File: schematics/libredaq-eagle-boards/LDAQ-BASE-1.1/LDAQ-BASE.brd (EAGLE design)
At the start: 130 x 101 mm, 111 parts, among them Q1 FDV301N, Q2 FDV301N, Q3 FDV301N, Q4 FDV301N, Q5 FDV301N, Q6 FDV301N, Q7 FDV301N, T1 FDN340P, U1 ATSAM3U1CB, U2 LM3671MF-3.3, U4 ISL3175, U6 MCP16322, U8 LMV321, X1 PJ-102A, Y1 12M

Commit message: update from local copy
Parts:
- removed D1: D1, diode:SMB
- removed U6: MCP16322, libredaq-comps:QFN16-3X3MM
- removed X1: PJ-102A, SmartPrj:POWERSUPPLY_DC-21MM
- added D2: FM4004W-W, FM4004W-W:DIOM5025X231N
- added J1: PJ-102A, PJ-102A:PJ-102AH
- added U3: TS30012-M050QFNR, TS30012-M050QFNR:QFN50P300X300X100-17N
- JP6: value SCREWTERMINAL-3.5MM-3 -> 691214110003; device libredaq-comps:SCREWTERMINAL-3.5MM-3 -> 691214110003:691214110003
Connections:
- removed net N$16: C10.2, L5.1, U6.1, U6.12, U6.13, U6.16
- new net FB_PWR5: C10.2, L5.1, U3.1, U3.12, U3.13, U3.16
- net +5V: now also U3.5; no longer U6.5
- net GND: now also J1.2, J1.3, U3.14, U3.15, U3.17; no longer U6.14, U6.15, U6.4, U6.EXT, X1.1, X1.3
- net N$17: now also U3.10; no longer U6.10
- net PWRIN: now also D2.2, J1.1; no longer D1.A, X1.2
- net VIN: now also D2.1, U3.11, U3.2, U3.3; no longer D1.C, U6.11, U6.2, U6.3
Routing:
- net N$16: track 29.1 -> 0.00 mm
- net FB_PWR5: track 0.00 -> 22.3 mm
- net GND: track 899.0 -> 885.3 mm

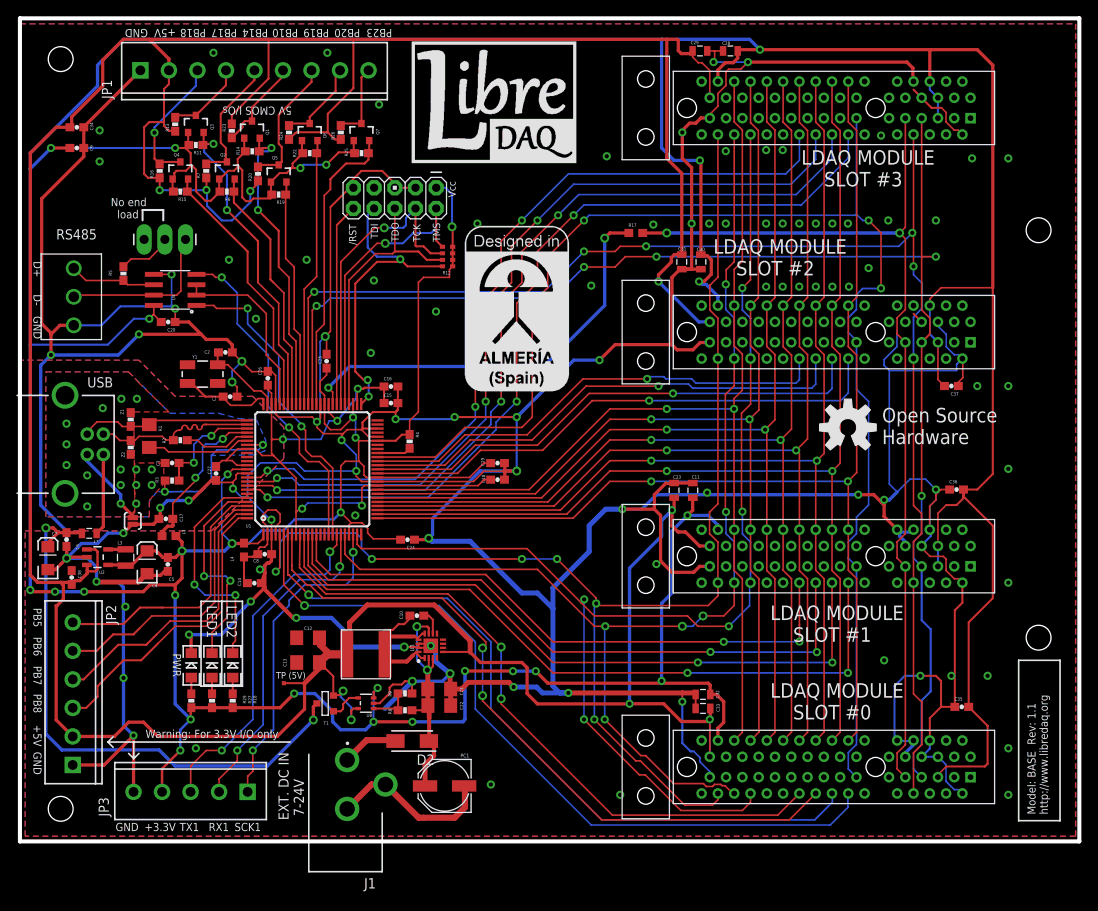
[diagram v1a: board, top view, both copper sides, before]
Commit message: base board: use bidirectional 3.3-5V driver
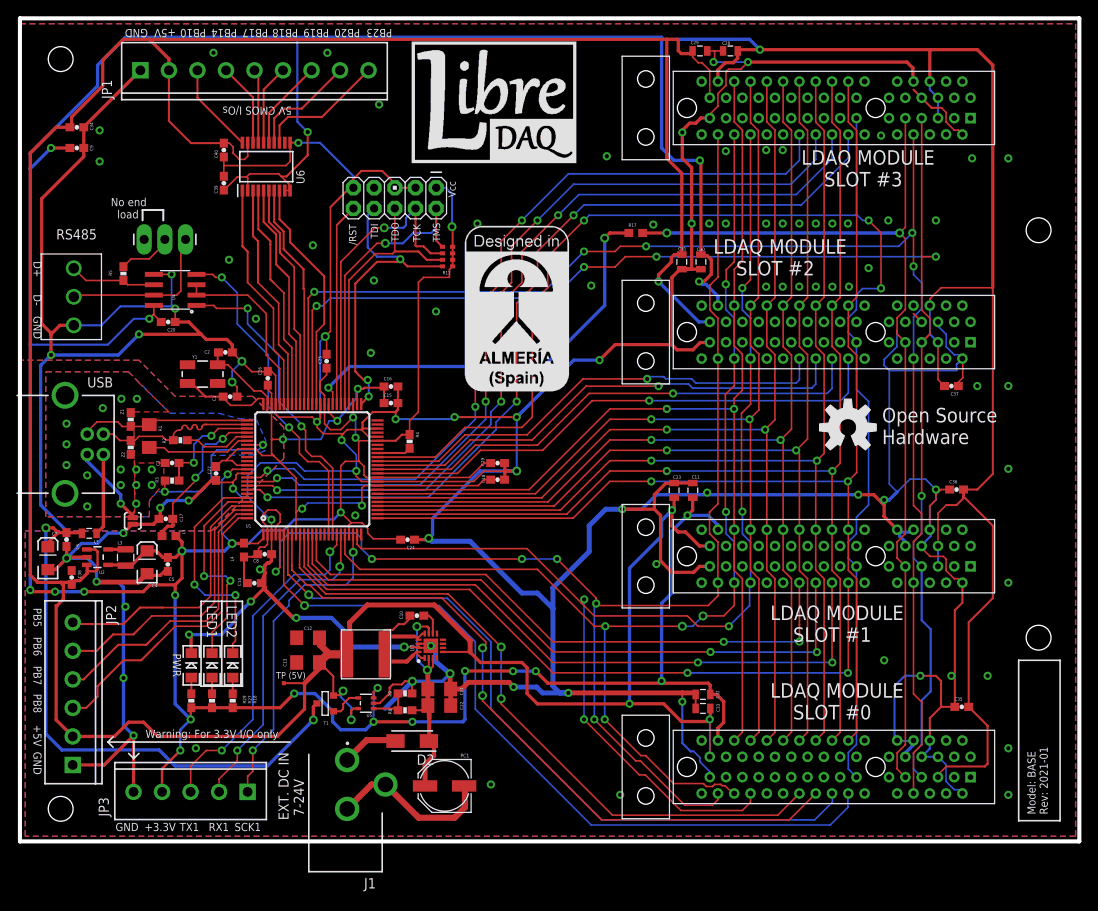
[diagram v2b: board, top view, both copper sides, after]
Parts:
- removed Q1, Q2, Q3, Q4, Q5, Q6, Q7: FDV301N, SparkFun:SOT23-3
- removed R11, R13, R14, R15, R16, R19, R20, R22, R23, R24, R25, R26, R6, R7: 10K, SparkFun:0603-RES
- added C39, C40: 0.1uF, SparkFun-Capacitors:0603-CAP
- added U6: TXB0108PWR, TXB0108PWR:SOP65P640X120-20N
- renumbered U8 to U5
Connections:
- net +5V: now also C40.1, U6.19; no longer R13.1, R16.1, R20.1, R23.1, R24.1, R26.1, R7.1
- net 3.3V: now also C39.1, U6.10, U6.2, U6.9; no longer Q1.1, Q2.1, Q3.1, Q4.1, Q5.1, Q6.1, Q7.1, R11.1, R14.1, R15.1, R19.1, R22.1, R25.1, R6.1
- net GND: now also C39.2, C40.2, U6.11
- net PB10_3.3: now also U6.1; no longer Q4.2, R15.2
- net PB10_5.0: now also JP1.3, U6.20; no longer JP1.6, Q1.3, R23.2
- net PB14_3.3: now also U6.3; no longer Q3.2, R11.2
- net PB14_5.0: now also JP1.4, U6.18; no longer JP1.5, Q2.3, R7.2
- net PB17_3.3: now also U6.4; no longer Q2.2, R6.2
- net PB17_5.0: now also JP1.5, U6.17; no longer JP1.4, Q3.3, R13.2
- net PB18_3.3: now also U6.5; no longer Q1.2, R14.2
- net PB18_5.0: now also JP1.6, U6.16; no longer JP1.3, Q4.3, R16.2
- net PB19_3.3: now also U6.6; no longer Q5.2, R19.2
- net PB19_5.0: now also U6.15; no longer Q5.3, R20.2
- net PB20_3.3: now also U6.7; no longer Q6.2, R22.2
- net PB20_5.0: now also U6.14; no longer Q6.3, R24.2
- net PB23_3.3: now also U6.8; no longer Q7.2, R25.2
- net PB23_5.0: now also U6.13; no longer Q7.3, R26.2
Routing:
- net +5V: track 467.6 -> 416.1 mm, vias 9 -> 6
- net 3.3V: track 779.4 -> 743.0 mm, vias 30 -> 28
- net GND: track 885.3 -> 909.2 mm, vias 99 -> 100
- net PB14_3.3: track 40.1 -> 28.0 mm, vias 2 -> 0
- net PB18_3.3: track 38.0 -> 27.9 mm, vias 2 -> 0
- net PB23_3.3: track 36.4 -> 28.9 mm
- net PB18_5.0: track 16.6 -> 9.86 mm, vias 1 -> 0
- net PB23_5.0: track 9.53 -> 15.8 mm
- net PB14_5.0: track 15.9 -> 10.3 mm
- net PB20_3.3: track 33.0 -> 27.7 mm
- net PB19_5.0: track 16.2 -> 11.0 mm
- net PB10_3.3: track 32.6 -> 28.3 mm
- net PB20_5.0: track 10.7 -> 14.3 mm
- net PB17_3.3: track 30.6 -> 27.9 mm
- net PB17_5.0: track 9.70 -> 9.07 mm
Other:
- board text added: "Model: BASE Rev: 2021-01"
- board text removed: "Model: BASE Rev: 1.1 http://www.libredaq.org"

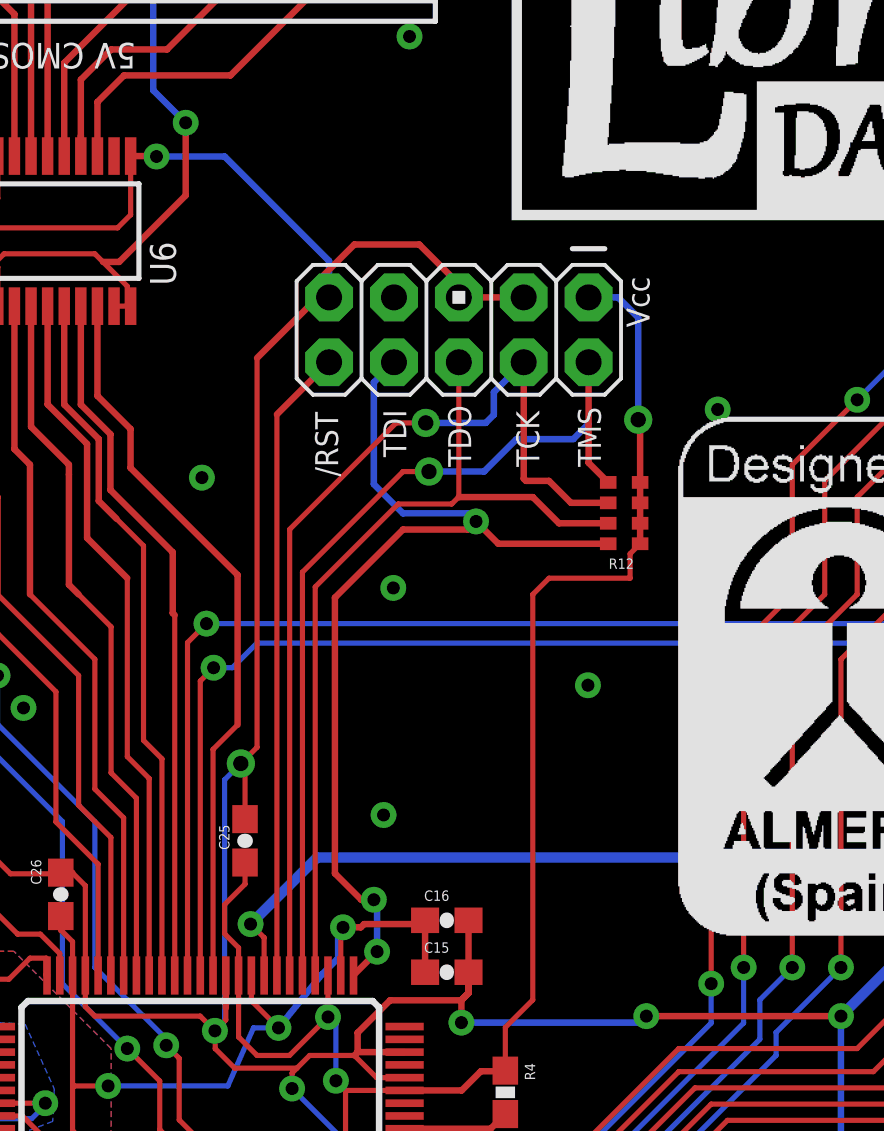
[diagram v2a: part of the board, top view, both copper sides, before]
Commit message: Base: Use JTAG 50mils connector
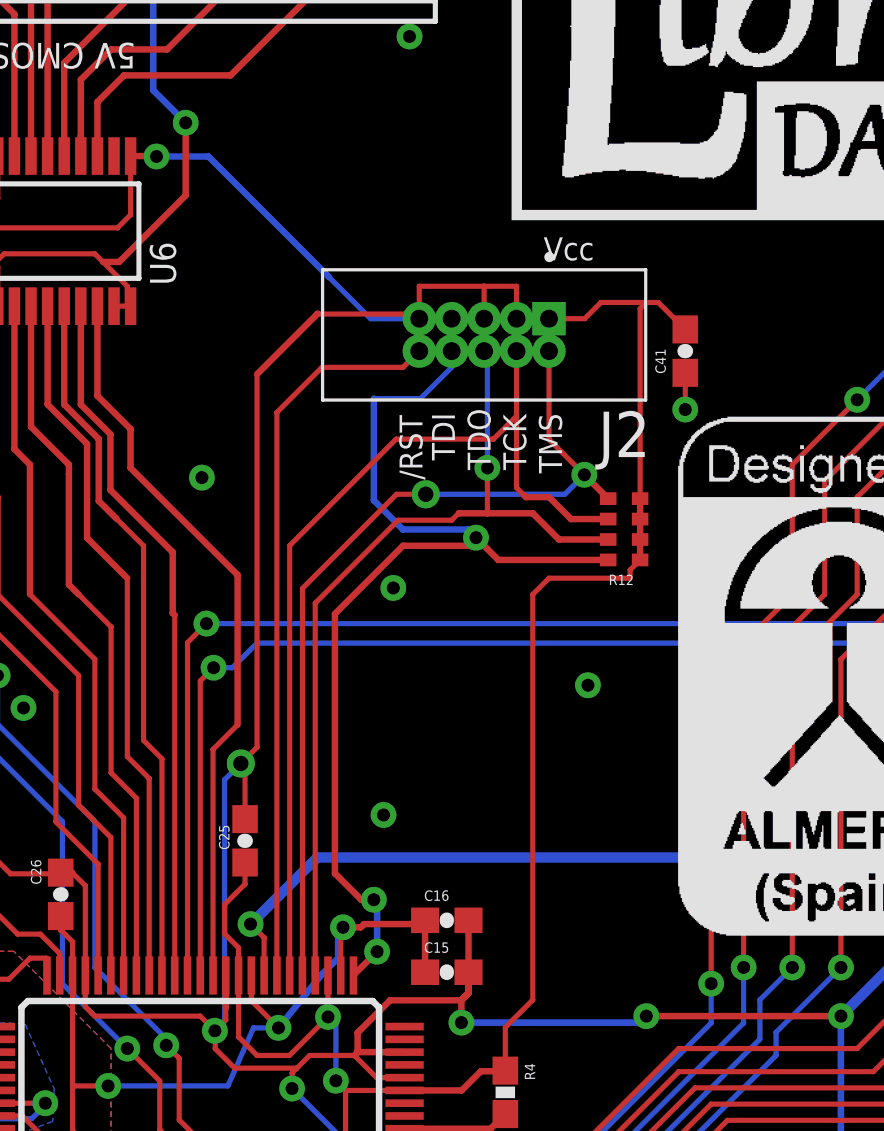
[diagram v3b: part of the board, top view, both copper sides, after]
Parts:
- removed JP4: SAM JTAG, SparkFun-Connectors:AVR_ICSP
- added C41: 0.1uF, SparkFun-Capacitors:0603-CAP
- added J2: 3221-10-0100-00, 3221-10-0100-00:CNC_3221-10-0100-00
- moved R12 0.64 mm to (52.5, 71.1)
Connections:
- net !JTAG_RESET: now also J2.10; no longer JP4.10
- net 3.3V: now also C41.2, J2.1; no longer JP4.1
- net GND: now also C41.1, J2.3, J2.5, J2.9; no longer JP4.3, JP4.5, JP4.9
- net JTAG_TCK: now also J2.4; no longer JP4.4
- net JTAG_TDI: now also J2.8; no longer JP4.8
- net JTAG_TDO: now also J2.6; no longer JP4.6
- net JTAG_TMS: now also J2.2; no longer JP4.2
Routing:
- net GND: track 909.2 -> 913.8 mm
- net 3.3V: track 743.0 -> 747.4 mm, vias 28 -> 27
- net !JTAG_RESET: track 24.9 -> 28.6 mm
- net JTAG_TMS: track 36.8 -> 34.8 mm, vias 1 -> 2
- net JTAG_TDI: track 38.5 -> 40.6 mm
- net JTAG_TCK: track 38.1 -> 37.3 mm, vias 1 -> 0
- net JTAG_TDO: track 33.8 -> 34.3 mm, vias 0 -> 1

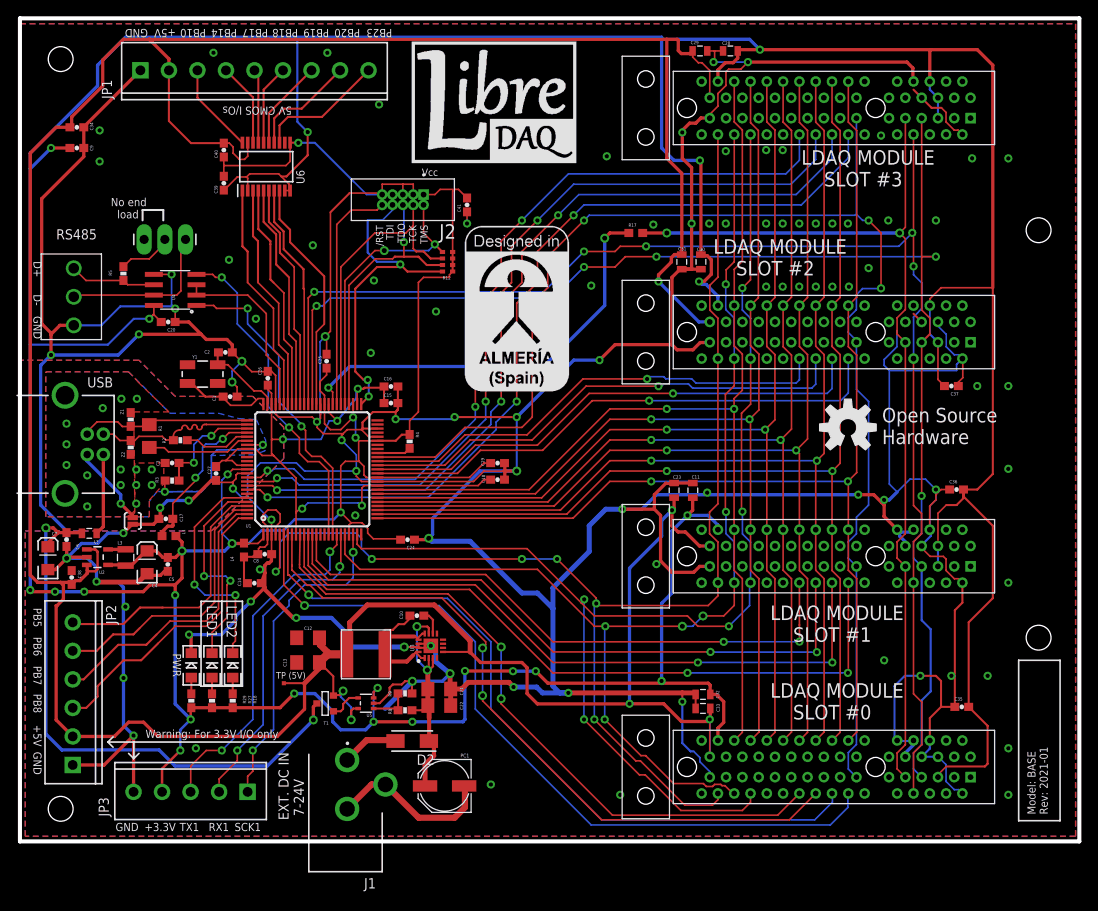
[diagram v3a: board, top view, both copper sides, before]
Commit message: Update connectors in BASE
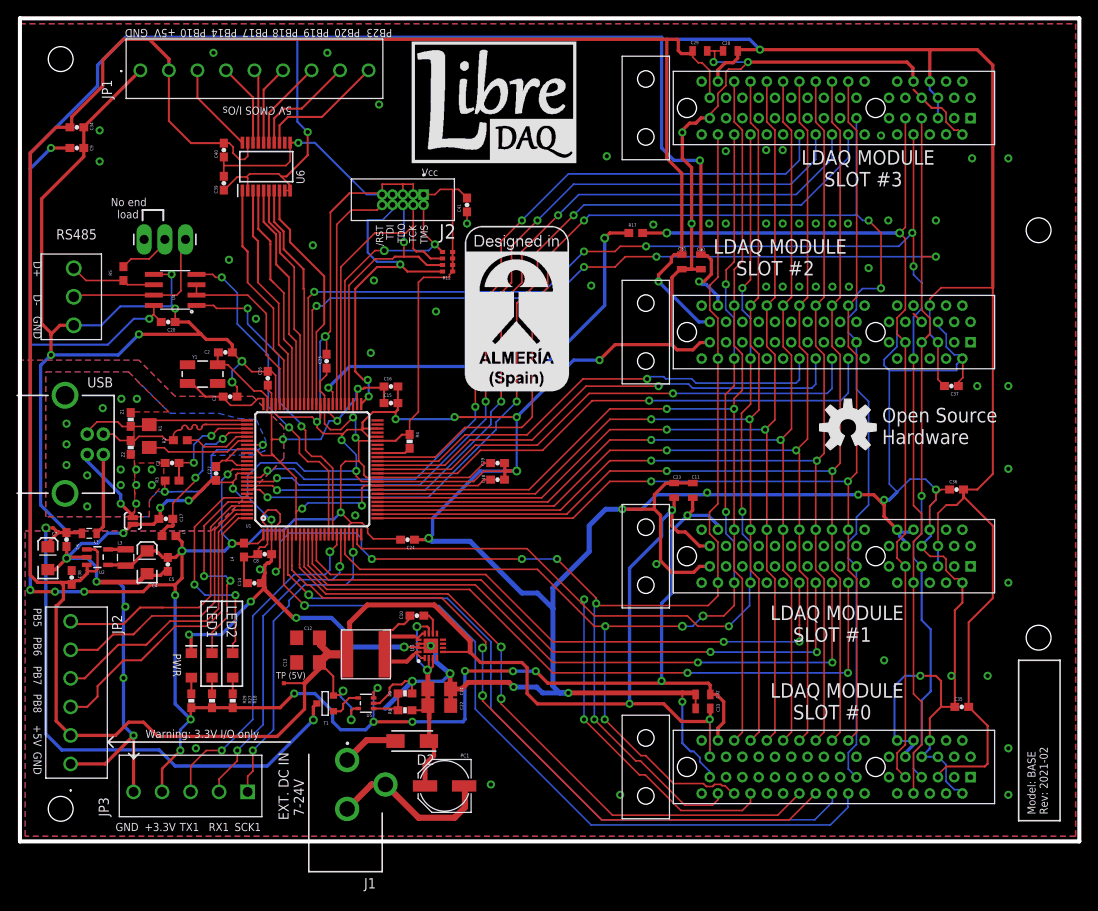
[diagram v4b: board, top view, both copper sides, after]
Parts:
- JP1: value SCREWTERMINAL-3.5MM-9 -> 39357-0009; device libredaq-comps:SCREWTERMINAL-3.5MM-9 -> SamacSys_Parts:393570009
- JP2: value SCREWTERMINAL-3.5MM-6 -> 1984659; device libredaq-comps:SCREWTERMINAL-3.5MM-6 -> SamacSys_Parts:1984659
- JP3: value SCREWTERMINAL-3.5MM-5 -> 1984646; device libredaq-comps:SCREWTERMINAL-3.5MM-5 -> SamacSys_Parts:1984646
- R1: value 39R 1% -> (none)
- R17: device SparkFun-Resistors:0603 -> SparkFun-Resistors:0603@1
- R2: value 39R 1% -> (none); device SparkFun-Resistors:0603-RES -> SparkFun-Resistors:0603
- R3: value 6K8 1% -> (none); device SparkFun-Resistors:0603-RES -> SparkFun-Resistors:0603
- R5: value 120R -> (none); device SparkFun-Resistors:0603-RES -> SparkFun-Resistors:0603
- moved JP2 0.28 mm to (6.22, 9.51)
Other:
- board text added: "Model: BASE Rev: 2021-02"
- board text added: "Warning: 3.3V I/O only"
- board text removed: "Model: BASE Rev: 2021-01"
- board text removed: "Warning: For 3.3V I/O only"

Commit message: optimized board size
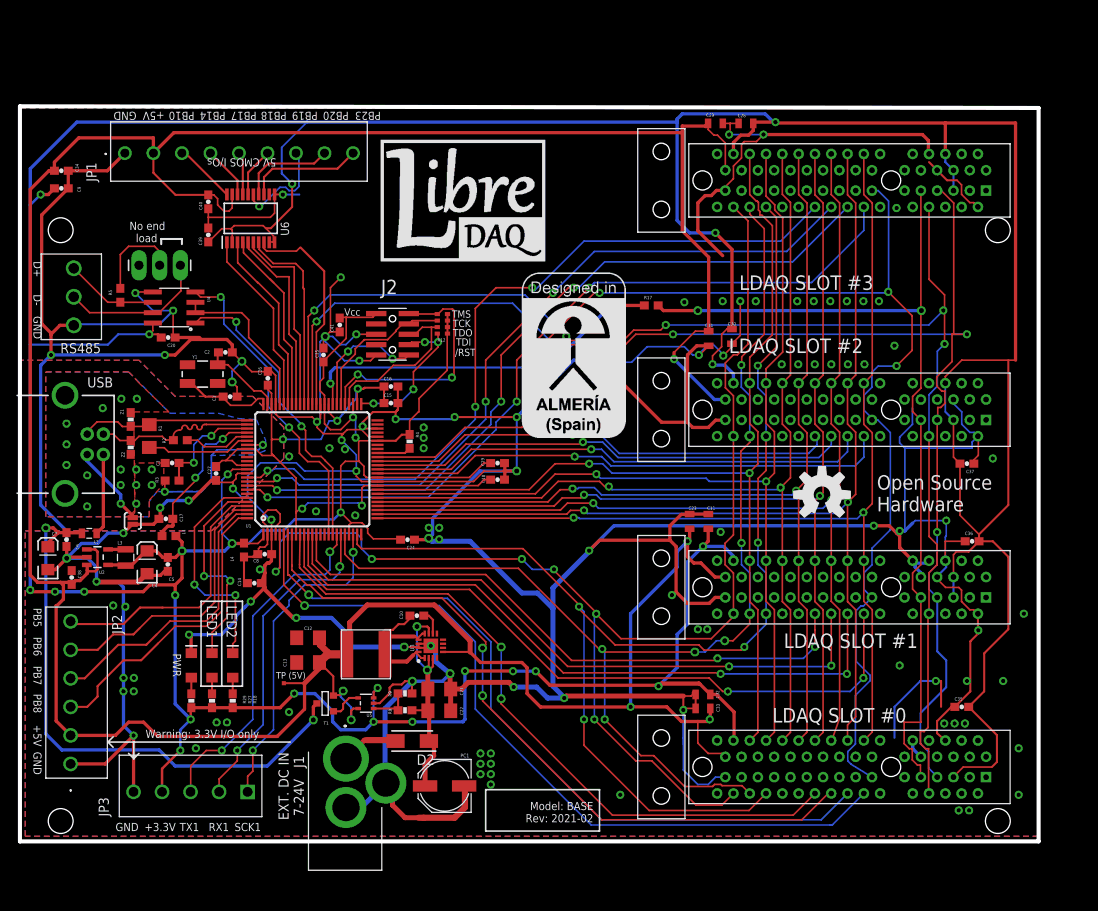
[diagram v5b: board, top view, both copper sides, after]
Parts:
- J1: value PJ-102A -> 4840.2211; device PJ-102A:PJ-102AH -> SamacSys_Parts:48402211
- J2: value 3221-10-0100-00 -> M50-3610542; device 3221-10-0100-00:CNC_3221-10-0100-00 -> SamacSys_Parts:M503610542
- moved U$3 23.0 mm to (120.0, 2.50)
- moved C41 21.5 mm to (39.2, 63.4)
- moved U$2 21.0 mm to (5.00, 75.0)
- moved J2 16.6 mm to (45.7, 62.2), turned to 270 degrees
- moved U$1 12.7 mm to (44.2, 71.2)
- moved JP1 10.3 mm to (12.9, 84.5)
- moved C31 9.96 mm to (84.5, 61.7)
- moved C30 9.91 mm to (87.4, 62.0)
- moved C37 9.71 mm to (116.2, 46.4)
- moved SLOT2 9.71 mm to (106.9, 53.0)
- moved C28 9.09 mm to (89.1, 88.1)
- moved C29 9.09 mm to (85.3, 88.1)
- moved R17 9.09 mm to (77.5, 65.8)
- moved SLOT3 9.09 mm to (106.9, 81.1)
- moved U$6 9.03 mm to (61.6, 49.5)
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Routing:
- net JTAG_TDI: track 40.6 -> 19.0 mm, vias 3 -> 4
- net +5V: track 416.1 -> 397.5 mm
- net JTAG_TCK: track 37.3 -> 19.1 mm
- net 3.3V: track 747.4 -> 729.9 mm
- net JTAG_TDO: track 34.3 -> 20.6 mm, vias 1 -> 0
- net !JTAG_RESET: track 28.6 -> 15.6 mm, vias 0 -> 2
- net GND: track 914.0 -> 901.6 mm, vias 100 -> 113
- net SLOT3_CTRL2: track 100.5 -> 90.6 mm
- net SLOT3_CTRL1: track 102.0 -> 92.6 mm
- net D5: track 134.5 -> 125.6 mm
- net D4: track 136.3 -> 127.5 mm
- net D2: track 139.8 -> 131.0 mm
- net LDAQ_RESET: track 170.3 -> 161.7 mm
- net D6: track 132.9 -> 124.4 mm
- net D0: track 143.1 -> 134.6 mm
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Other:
- board size 130 x 101 mm -> 125 x 90.2 mm
- board text added: "LDAQ SLOT #0"
- board text added: "LDAQ SLOT #1"
- board text added: "LDAQ SLOT #2"
- board text added: "LDAQ SLOT #3"
- board text removed: "LDAQ MODULE SLOT #0"
- board text removed: "LDAQ MODULE SLOT #1"
- board text removed: "LDAQ MODULE SLOT #2"
- board text removed: "LDAQ MODULE SLOT #3"
